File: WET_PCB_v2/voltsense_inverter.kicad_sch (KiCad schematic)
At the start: 10 parts, among them J17 Capacitor connector, J19 Capacitor connector, U3 Opamp_Quad

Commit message: microcontroller to chip traces done
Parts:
- added R21: R0, Resistor_SMD:R_0805_2012Metric_Pad1.20x1.40mm_HandSolder, symbol Device:R
- D10: renamed from D31; footprint Diode_THT:D_DO-15_P2.54mm_Vertical_CathodeUp -> Diode_SMD:D_SMF
- D11: renamed from D32; footprint Diode_THT:D_DO-15_P2.54mm_Vertical_CathodeUp -> Diode_SMD:D_SMF
- J13: renamed from J19; footprint Connector_PinSocket_2.54mm:PinSocket_1x02_P2.54mm_Vertical -> Connector_PinSocket_2.54mm:PinSocket_1x02_P2.54mm_Horizontal
- J14: renamed from J17; footprint Connector_PinSocket_2.54mm:PinSocket_1x02_P2.54mm_Vertical -> Connector_PinSocket_2.54mm:PinSocket_1x02_P2.54mm_Horizontal
- renumbered R1 to R30, R2 to R31, R3 to R32, R41 to R33, R4 to R34, U3 to U1
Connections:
- net GND: now also J13.2 (Pin_2); no longer J13.1 (Pin_1)
- net Vsense_ADC: now also R21.2; no longer J14.2 (Pin_2), R34.2
- net at R30.2, R31.1, R32.1: now also J13.1 (Pin_1); no longer J13.2 (Pin_2)
- new net: J14.2 (Pin_2), R21.1, R34.2
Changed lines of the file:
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@@
+	(wire
+		(pts
+			(xy 127 50.8) (xy 128.27 50.8)
+		)
+		(stroke
+			(width 0)
+			(type default)
+		)
+	)
 	(wire
 		(pts
@@
 	(wire
 		(pts
-			(xy 118.11 50.8) (xy 128.27 50.8)
+			(xy 118.11 50.8) (xy 119.38 50.8)
 		)
 		(stroke
@@
 		(in_pos_files yes)
 		(dnp no)
-		(property "Reference" "J17"
+		(property "Reference" "J14"
 			(at 120.65 55.8799 90)
 			(show_name no)
@@
 			)
 		)
-		(property "Footprint" "Connector_PinSocket_2.54mm:PinSocket_1x02_P2.54mm_Vertical"
+		(property "Footprint" "Connector_PinSocket_2.54mm:PinSocket_1x02_P2.54mm_Horizontal"
 			(at 118.11 58.42 0)
 			(hide yes)
@@
 			(project "WET_PCB_v2"
 				(path "/13451c35-1666-47d9-9525-8d8125ba1cf3/419c9796-b7e1-43c1-b033-dc2479750a67"
-					(reference "J17")
+					(reference "J14")
 					(unit 1)
 				)
@@
 		(dnp no)
 		(fields_autoplaced yes)
-		(property "Reference" "R4"
+		(property "Reference" "R34"
 			(at 110.49 44.45 90)
 			(show_name no)
@@
 			(project "WET_PCB_v2"
 				(path "/13451c35-1666-47d9-9525-8d8125ba1cf3/419c9796-b7e1-43c1-b033-dc2479750a67"
-					(reference "R4")
+					(reference "R34")
 					(unit 1)
 				)
@@
 		(dnp no)
 		(fields_autoplaced yes)
-		(property "Reference" "R2"
+		(property "Reference" "R31"
 			(at 55.88 54.6099 0)
 			(show_name no)
@@
 			(project "WET_PCB_v2"
 				(path "/13451c35-1666-47d9-9525-8d8125ba1cf3/419c9796-b7e1-43c1-b033-dc2479750a67"
-					(reference "R2")
+					(reference "R31")
 					(unit 1)
 				)
@@
 		(dnp no)
 		(fields_autoplaced yes)
-		(property "Reference" "D31"
+		(property "Reference" "D10"
 			(at 130.81 44.4499 90)
 			(show_name no)
@@
 			)
 		)
-		(property "Footprint" "Diode_THT:D_DO-15_P2.54mm_Vertical_CathodeUp"
+		(property "Footprint" "Diode_SMD:D_SMF"
 			(at 128.27 45.72 0)
 			(hide yes)
@@
 			(project "WET_PCB_v2"
 				(path "/13451c35-1666-47d9-9525-8d8125ba1cf3/419c9796-b7e1-43c1-b033-dc2479750a67"
-					(reference "D31")
+					(reference "D10")
 					(unit 1)
 				)
@@
 	(symbol
 		(lib_id "Connector_Generic:Conn_02x01")
-		(at 62.23 57.15 90)
+		(at 62.23 54.61 90)
+		(mirror x)
 		(unit 1)
 		(body_style 1)
@@
 		(in_pos_files yes)
 		(dnp no)
-		(property "Reference" "J19"
-			(at 64.77 54.6099 90)
+		(property "Reference" "J13"
+			(at 64.77 57.1501 90)
 			(show_name no)
 			(do_not_autoplace no)
@@
 			)
 		)
-		(property "Footprint" "Connector_PinSocket_2.54mm:PinSocket_1x02_P2.54mm_Vertical"
-			(at 62.23 57.15 0)
+		(property "Footprint" "Connector_PinSocket_2.54mm:PinSocket_1x02_P2.54mm_Horizontal"
+			(at 62.23 54.61 0)
 			(hide yes)
 			(show_name no)
@@
 		)
 		(property "Datasheet" ""
-			(at 62.23 57.15 0)
+			(at 62.23 54.61 0)
 			(hide yes)
 			(show_name no)
@@
 		)
 		(property "Description" "Generic connector, double row, 02x01, this symbol is compatible with counter-clockwise, top-bottom and odd-even numbering schemes., script generated (kicad-library-utils/schlib/autogen/connector/)"
-			(at 62.23 57.15 0)
+			(at 62.23 54.61 0)
 			(hide yes)
 			(show_name no)
@@
 			(project "WET_PCB_v2"
 				(path "/13451c35-1666-47d9-9525-8d8125ba1cf3/419c9796-b7e1-43c1-b033-dc2479750a67"
-					(reference "J19")
+					(reference "J13")
 					(unit 1)
 				)
@@
 		(dnp no)
 		(fields_autoplaced yes)
-		(property "Reference" "#PWR018"
+		(property "Reference" "#PWR041"
 			(at 62.23 68.58 0)
 			(hide yes)
@@
 			(project "WET_PCB_v2"
 				(path "/13451c35-1666-47d9-9525-8d8125ba1cf3/419c9796-b7e1-43c1-b033-dc2479750a67"
-					(reference "#PWR018")
+					(reference "#PWR041")
 					(unit 1)
 				)
@@
 		(dnp no)
 		(fields_autoplaced yes)
-		(property "Reference" "R3"
+		(property "Reference" "R32"
 			(at 69.85 41.91 90)
 			(show_name no)
@@
 			(project "WET_PCB_v2"
 				(path "/13451c35-1666-47d9-9525-8d8125ba1cf3/419c9796-b7e1-43c1-b033-dc2479750a67"
-					(reference "R3")
+					(reference "R32")
 					(unit 1)
 				)
@@
 		(in_pos_files yes)
 		(dnp no)
-		(property "Reference" "U3"
+		(property "Reference" "U1"
 			(at 91.44 46.736 0)
 			(show_name no)
@@
 			(project "WET_PCB_v2"
 				(path "/13451c35-1666-47d9-9525-8d8125ba1cf3/419c9796-b7e1-43c1-b033-dc2479750a67"
-					(reference "U3")
+					(reference "U1")
 					(unit 2)
 				)
@@
 		(dnp no)
 		(fields_autoplaced yes)
-		(property "Reference" "D32"
+		(property "Reference" "D11"
 			(at 130.81 54.6099 90)
 			(show_name no)
@@
 			)
 		)
-		(property "Footprint" "Diode_THT:D_DO-15_P2.54mm_Vertical_CathodeUp"
+		(property "Footprint" "Diode_SMD:D_SMF"
 			(at 128.27 55.88 0)
 			(hide yes)
@@
 			(project "WET_PCB_v2"
 				(path "/13451c35-1666-47d9-9525-8d8125ba1cf3/419c9796-b7e1-43c1-b033-dc2479750a67"
-					(reference "D32")
+					(reference "D11")
 					(unit 1)
 				)
@@
 		(in_pos_files yes)
 		(dnp no)
-		(property "Reference" "#PWR022"
+		(property "Reference" "#PWR043"
 			(at 128.27 66.04 0)
 			(hide yes)
@@
 			(project "WET_PCB_v2"
 				(path "/13451c35-1666-47d9-9525-8d8125ba1cf3/419c9796-b7e1-43c1-b033-dc2479750a67"
-					(reference "#PWR022")
+					(reference "#PWR043")
 					(unit 1)
 				)
@@
 		(dnp no)
 		(fields_autoplaced yes)
-		(property "Reference" "R41"
+		(property "Reference" "R33"
 			(at 91.44 52.07 90)
 			(show_name no)
@@
 			(project "WET_PCB_v2"
 				(path "/13451c35-1666-47d9-9525-8d8125ba1cf3/419c9796-b7e1-43c1-b033-dc2479750a67"
-					(reference "R41")
+					(reference "R33")
 					(unit 1)
 				)
@@
 		(in_pos_files yes)
 		(dnp no)
-		(property "Reference" "#PWR021"
+		(property "Reference" "#PWR042"
 			(at 118.11 69.85 0)
 			(hide yes)
@@
 			(project "WET_PCB_v2"
 				(path "/13451c35-1666-47d9-9525-8d8125ba1cf3/419c9796-b7e1-43c1-b033-dc2479750a67"
-					(reference "#PWR021")
+					(reference "#PWR042")
 					(unit 1)
 				)
@@
 		(dnp no)
 		(fields_autoplaced yes)
-		(property "Reference" "R1"
+		(property "Reference" "R30"
 			(at 55.88 38.0999 0)
 			(show_name no)
@@
 			(project "WET_PCB_v2"
 				(path "/13451c35-1666-47d9-9525-8d8125ba1cf3/419c9796-b7e1-43c1-b033-dc2479750a67"
-					(reference "R1")
+					(reference "R30")
 					(unit 1)
 				)
@@
 		(dnp no)
 		(fields_autoplaced yes)
-		(property "Reference" "#PWR017"
+		(property "Reference" "#PWR040"
 			(at 53.34 68.58 0)
 			(hide yes)
@@
 			(project "WET_PCB_v2"
 				(path "/13451c35-1666-47d9-9525-8d8125ba1cf3/419c9796-b7e1-43c1-b033-dc2479750a67"
-					(reference "#PWR017")
+					(reference "#PWR040")
 					(unit 1)
 				)
+			)
+		)
+	)
+	(symbol
+		(lib_id "Device:R")
+		(at 123.19 50.8 90)
+		(unit 1)
+		(body_style 1)
+		(exclude_from_sim no)
+		(in_bom yes)
+		(on_board yes)
+		(in_pos_files yes)
+		(dnp no)
+		(fields_autoplaced yes)
+		(property "Reference" "R21"
+			(at 123.19 44.45 90)
+			(show_name no)
+			(do_not_autoplace no)
+			(effects
+				(font
+					(size 1.27 1.27)
+				)
+			)
+		)
+		(property "Value" "R0"
+			(at 123.19 46.99 90)
+			(show_name no)
+			(do_not_autoplace no)
+			(effects
+				(font
+					(size 1.27 1.27)
+				)
+			)
+		)
+		(property "Footprint" "Resistor_SMD:R_0805_2012Metric_Pad1.20x1.40mm_HandSolder"
+			(at 123.19 52.578 90)
+			(hide yes)
+			(show_name no)
+			(do_not_autoplace no)
+			(effects
+				(font
+					(size 1.27 1.27)
+				)
+			)
+		)
+		(property "Datasheet" ""
+			(at 123.19 50.8 0)
+			(hide yes)
+			(show_name no)
+			(do_not_autoplace no)
+			(effects
+				(font
+					(size 1.27 1.27)
+				)
+			)
+		)
+		(property "Description" "Resistor"
+			(at 123.19 50.8 0)
+			(hide yes)
+			(show_name no)
+			(do_not_autoplace no)
+			(effects
+				(font
+					(size 1.27 1.27)
+				)
+			)
+		)
+		(pin "2"
+		)
+		(pin "1"
+		)
+		(instances
+			(project "WET_PCB_v2"
+				(path "/13451c35-1666-47d9-9525-8d8125ba1cf3/419c9796-b7e1-43c1-b033-dc2479750a67"
+					(reference "R21")
+					(unit 1)
+				)

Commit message: labels
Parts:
- renumbered R33 to JMP18, R21 to JMP19
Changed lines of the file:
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@@
 		(dnp no)
 		(fields_autoplaced yes)
-		(property "Reference" "R33"
+		(property "Reference" "JMP18"
 			(at 91.44 52.07 90)
 			(show_name no)
@@
 			(project "WET_PCB_v2"
 				(path "/13451c35-1666-47d9-9525-8d8125ba1cf3/419c9796-b7e1-43c1-b033-dc2479750a67"
-					(reference "R33")
+					(reference "JMP18")
 					(unit 1)
 				)
@@
 		(dnp no)
 		(fields_autoplaced yes)
-		(property "Reference" "R21"
+		(property "Reference" "JMP19"
 			(at 123.19 44.45 90)
 			(show_name no)
@@
 			(project "WET_PCB_v2"
 				(path "/13451c35-1666-47d9-9525-8d8125ba1cf3/419c9796-b7e1-43c1-b033-dc2479750a67"
-					(reference "R21")
-					(unit 1)
-				)
+					(reference "JMP19")
+					(unit 1)
+				)

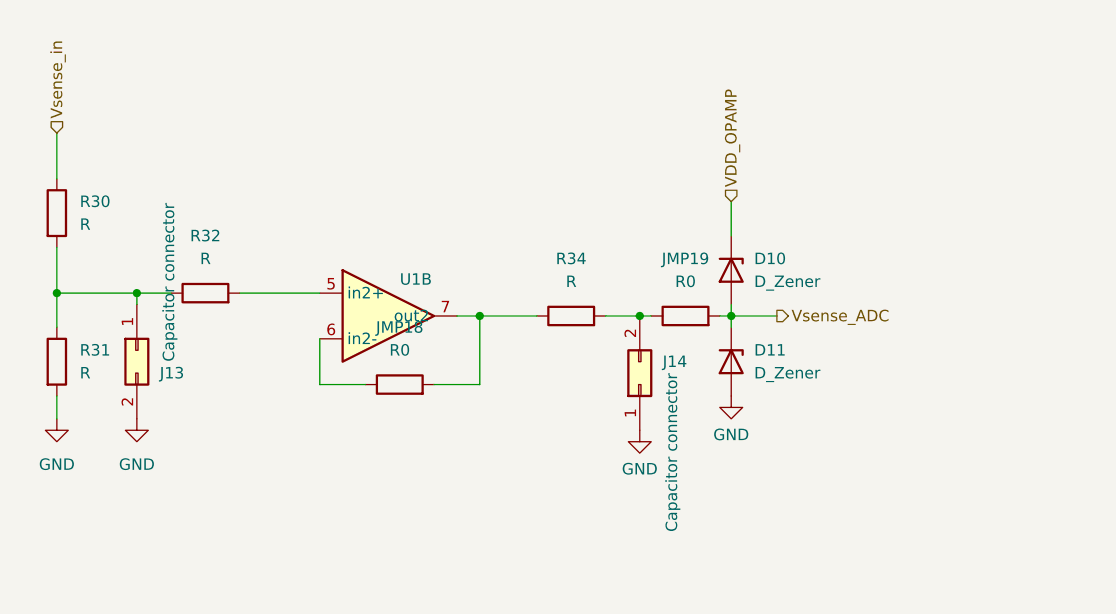
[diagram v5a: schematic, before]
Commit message: added values and notes for assembly
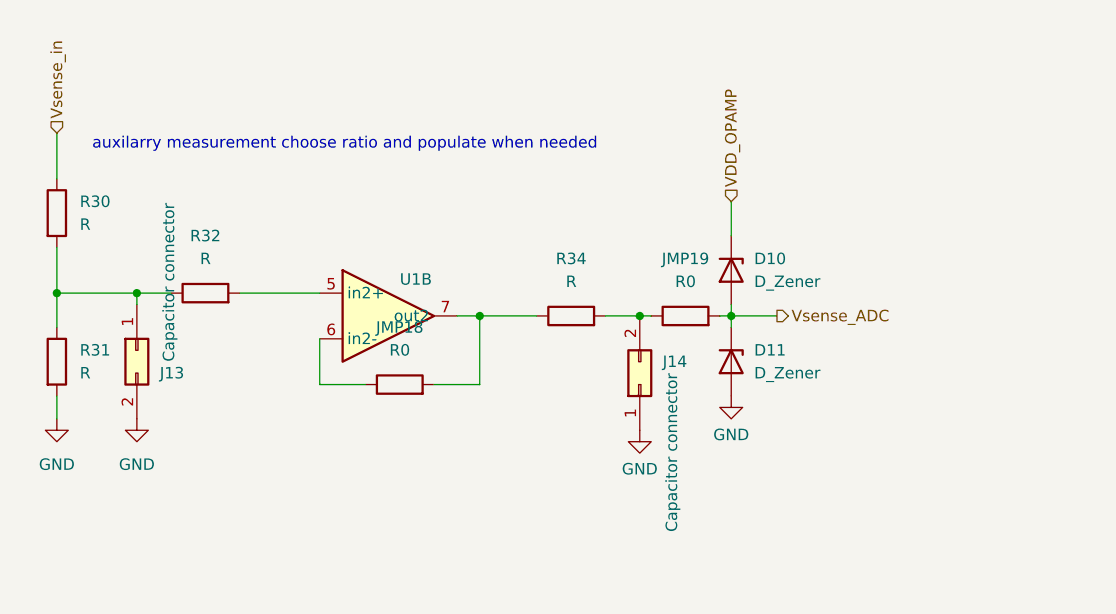
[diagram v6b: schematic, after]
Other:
- note added: "auxilarry measurement choose ratio and populate when needed"
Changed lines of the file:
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@@
 	(generator_version "10.0")
 	(paper "A4")
+	(text "auxilarry measurement choose ratio and populate when needed"
+		(exclude_from_sim no)
+		(at 85.344 31.75 0)
+		(effects
+			(font
+				(size 1.27 1.27)
+			)
+		)
+	)
 	(junction
 		(at 53.34 48.26)
